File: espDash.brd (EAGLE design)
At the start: 100 x 80 mm, 13 parts

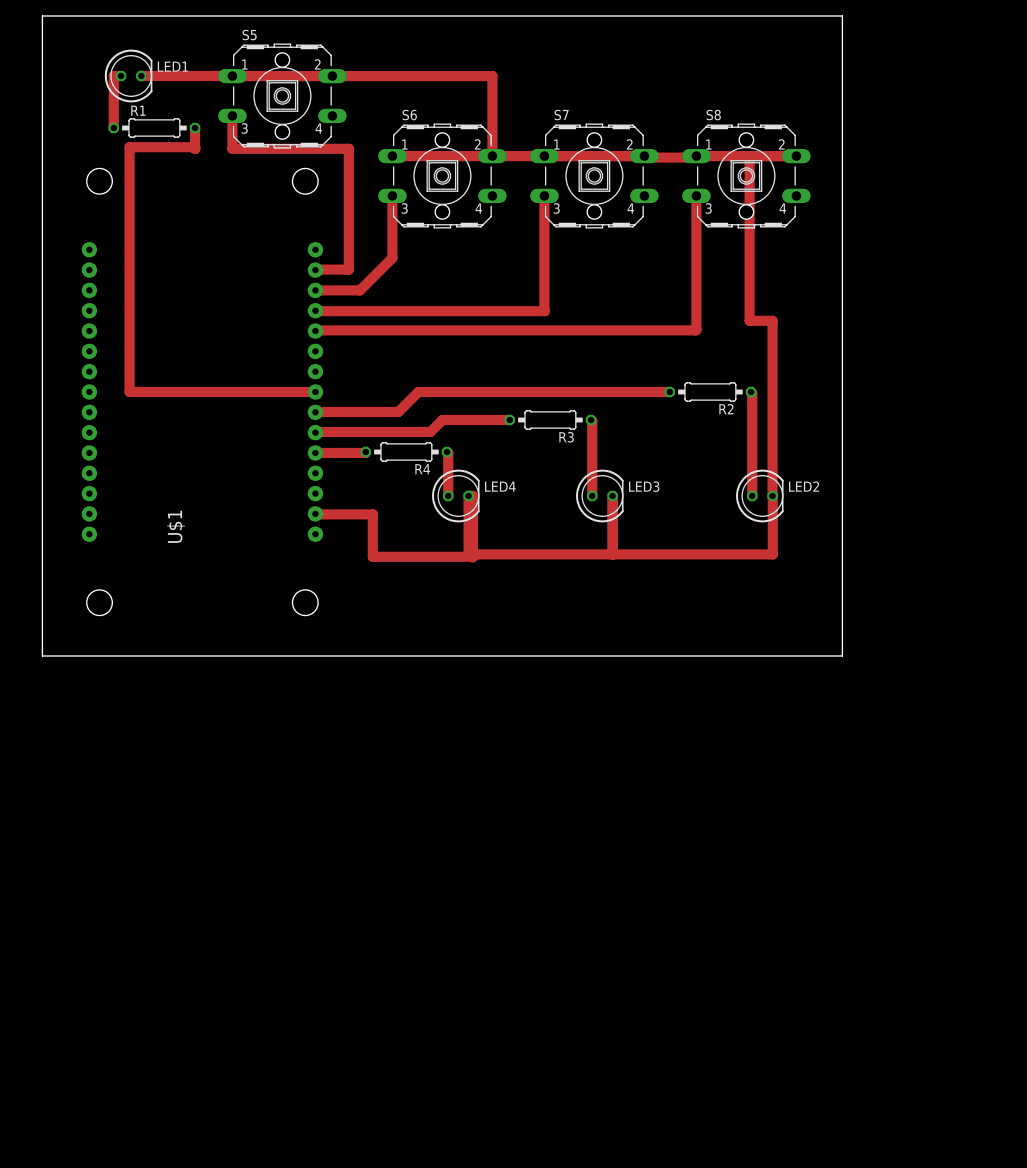
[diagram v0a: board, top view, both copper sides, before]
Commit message: 5 button
Added a button
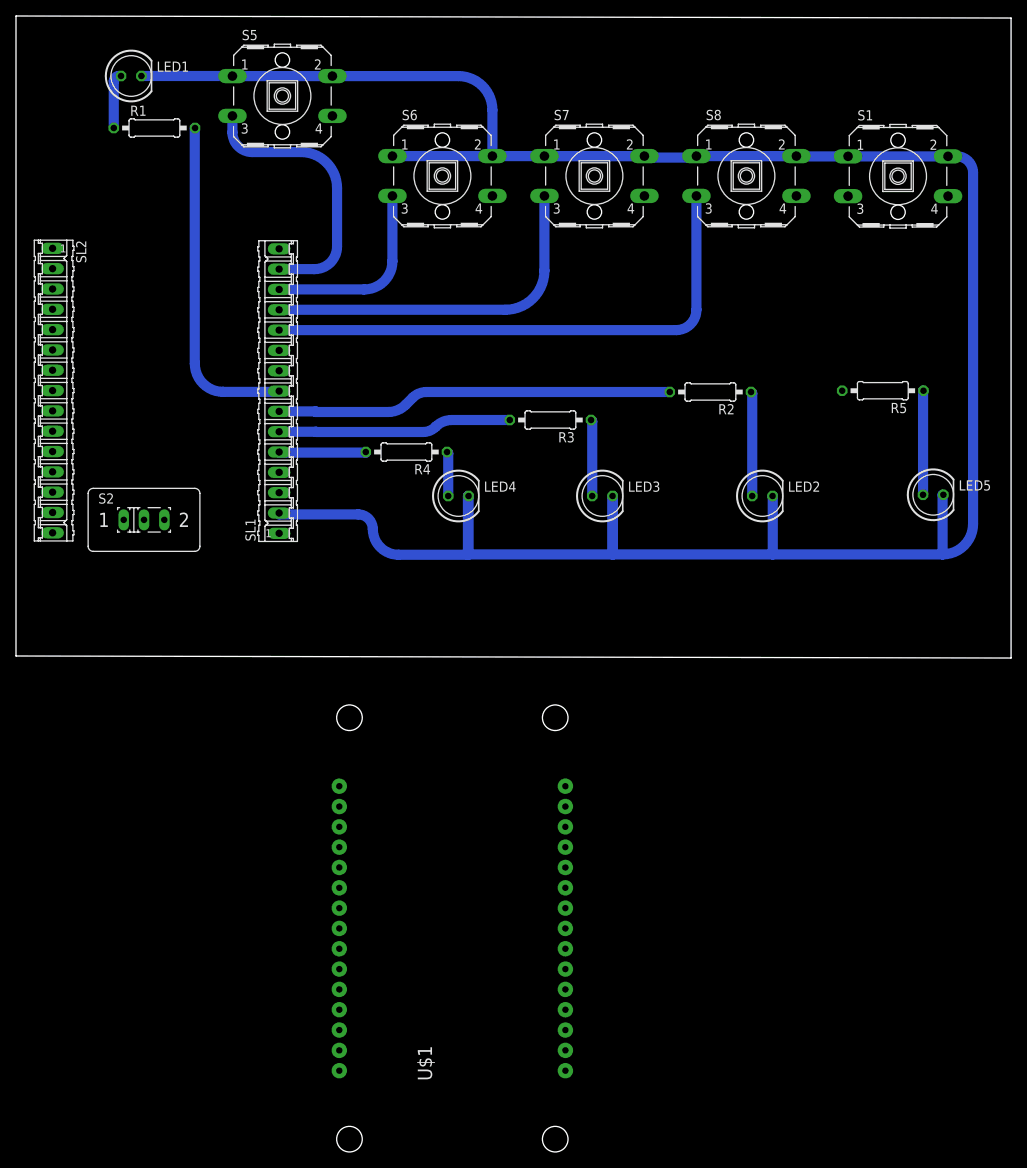
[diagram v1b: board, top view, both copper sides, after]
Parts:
- added LED5: (no value), led:LED5MM
- added R5: (no value), rcl:0207/10
- added S1: (no value), switch-omron:B3F-40XX
- added S2: (no value), switch:M251
- added SL1, SL2: (no value), con-amp-quick:15P
- moved U$1 74.0 mm to (51.2, -34.1)
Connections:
- new net N$14: LED5.A, R5.1
- net +3V3: now also SL2.11; no longer U$1.3V3@0
- net GND: now also LED5.K, S1.1, S1.2, SL1.2; no longer U$1.GND@3
- net N$1: now also SL1.14; no longer U$1.D1
- net N$2: now also SL1.13; no longer U$1.D2
- net N$3: now also SL1.12; no longer U$1.D3
- net N$4: now also SL1.11; no longer U$1.D4
- net N$5: now also SL1.8; no longer U$1.D5
- net N$6: now also SL1.7; no longer U$1.D6
- net N$7: now also SL1.6; no longer U$1.D7
- net N$8: now also SL1.5; no longer U$1.D8
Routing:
- net GND: track 264.5 -> 309.7 mm, vias 0 -> 1
- net N$5: track 64.9 -> 41.6 mm
- net N$14: track 0.00 -> 13.1 mm
- net N$2: track 19.1 -> 23.8 mm
- net N$8: track 6.41 -> 11.0 mm
- net N$6: track 45.3 -> 49.6 mm
- net N$7: track 24.9 -> 29.2 mm
- net N$1: track 38.0 -> 33.7 mm
- net N$4: track 64.4 -> 67.4 mm
- net N$3: track 43.1 -> 44.5 mm
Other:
- board size 100 x 80 mm -> 124.4 x 80.3 mm
